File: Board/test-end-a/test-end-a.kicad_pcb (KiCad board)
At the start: 2 copper layers, 150 x 80 mm, 37 parts, among them J10 SW2, J11 TENDA_2, J12 TENDA_1, J2 I2C connector, J5 VAC 230V, J6 VDC 5V, J7 SW1, J8 Anemometer, J9 TX RX - + Serial TTL, K1 FINDER-36.11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

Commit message: [ADD] Add consumption scheme and components on the board
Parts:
- added ACS1: JUMP, Jumper:SolderJumper-2_P1.3mm_Open_RoundedPad1.0x1.5mm, F.Cu at (192.4, 95.0)
- added C3: 1nF, Inductor_SMD:L_1206_3216Metric_Pad1.22x1.90mm_HandSolder, F.Cu at (198.7, 100.6)
- added C4: 56uF, Capacitor_THT:CP_Radial_D10.0mm_P5.00mm, F.Cu at (191.3, 111.8)
- added D4: 1N4148W, Diode_SMD:D_SOD-123, F.Cu at (198.6, 104.0)
- added R13: R100, Resistor_SMD:R_1206_3216Metric, F.Cu at (175.0, 120.1)
- added R14: R10k, Resistor_SMD:R_1206_3216Metric, F.Cu at (178.3, 120.1)
- added R15: R12k, Resistor_SMD:R_1206_3216Metric, F.Cu at (181.6, 120.1)
- added R16: R12k, Resistor_SMD:R_1206_3216Metric, F.Cu at (184.9, 120.1)
- added R17: R10k, Resistor_SMD:R_1206_3216Metric, F.Cu at (188.2, 120.1)
- added R18: R470, Resistor_SMD:R_1206_3216Metric, F.Cu at (191.6, 120.1)
- added R19: R180, Resistor_SMD:R_1206_3216Metric, F.Cu at (194.9, 120.1)
- added U4: ACS712xLCTR-05B, Package_SO:SOIC-8_3.9x4.9mm_P1.27mm, F.Cu at (203.5, 94.0)
- added U5: LM358, Package_SO:SOIC-8-1EP_3.9x4.9mm_P1.27mm_EP2.29x3mm, F.Cu at (211.3, 97.7)
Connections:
- J11 pad 2: /230V_N -> /230V_N_TENDA
- J12 pad 1: /230V_N -> /230V_N_TENDA
- U1 pad 8: unconnected-(U1-IO32-Pad8) -> /ampmeter
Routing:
- net /ampmeter: track 0.00 -> 217.4 mm, vias 0 -> 2
- net /230V_N_TENDA: track 0.00 -> 112.6 mm, vias 0 -> 1
- net GND: track 357.2 -> 467.5 mm, vias 4 -> 5
- net Net-(U4-VIOUT): track 0.00 -> 83.6 mm
- net +5V: track 167.3 -> 238.7 mm, vias 0 -> 5
- net Net-(U5A-+): track 0.00 -> 67.1 mm, vias 0 -> 2
- net Net-(D4-A): track 0.00 -> 62.1 mm
- net Net-(U5A--): track 0.00 -> 58.2 mm, vias 0 -> 2
- net /230V_N: track 115.9 -> 78.9 mm, vias 0 -> 1
- net Net-(D4-K): track 0.00 -> 36.9 mm, vias 0 -> 2
- net Net-(U4-FILTER): track 0.00 -> 11.4 mm
- net Net-(R17-Pad2): track 0.00 -> 7.88 mm, vias 0 -> 2
- net /230V_L: track 100.3 -> 102.9 mm

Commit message: [ENH] Move a wire to avoid interferences with high voltage
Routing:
- net GND: track 467.5 -> 439.1 mm, vias 5 -> 7
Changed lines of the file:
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@@
 			(psa4output no)
 			(plot_black_and_white yes)
+			(plotinvisibletext no)
 			(sketchpadsonfab no)
 			(plotpadnumbers no)
@@
 	)
 	(segment
-		(start 170.615999 133.281)
-		(end 128.281 133.281)
-		(width 0.2)
-		(layer "F.Cu")
-		(net 1)
-	)
-	(segment
 		(start 125.87224 73.46)
 		(end 127.5 73.46)
@@
 	)
 	(segment
-		(start 128.281 133.281)
-		(end 126 131)
-		(width 0.2)
-		(layer "F.Cu")
-		(net 1)
-	)
-	(segment
 		(start 125.6 97.6)
 		(end 122 94)
@@
 	)
 	(segment
-		(start 181.626 121.543)
-		(end 181.626 122.270999)
-		(width 0.2)
-		(layer "F.Cu")
-		(net 1)
-	)
-	(segment
 		(start 205.994 97.748999)
 		(end 206.1415 97.8965)
@@
 	)
 	(segment
+		(start 173.43 121.69066)
+		(end 173.43 111.304)
+		(width 0.2)
+		(layer "F.Cu")
+		(net 1)
+	)
+	(segment
+		(start 180.7625 122.4065)
+		(end 174.14584 122.4065)
+		(width 0.2)
+		(layer "F.Cu")
+		(net 1)
+	)
+	(segment
 		(start 114 131)
 		(end 111.719 133.281)
@@
 	)
 	(segment
+		(start 181.626 121.543)
+		(end 180.7625 122.4065)
+		(width 0.2)
+		(layer "F.Cu")
+		(net 1)
+	)
+	(segment
 		(start 117 86)
 		(end 117 85)
@@
 	)
 	(segment
+		(start 173.43 111.304)
+		(end 175.006 109.728)
+		(width 0.2)
+		(layer "F.Cu")
+		(net 1)
+	)
+	(segment
 		(start 116 117)
 		(end 116.5 117.5)
@@
 	(segment
 		(start 180.605008 99.051)
-		(end 175.848918 99.051)
+		(end 177.546 99.051)
 		(width 0.2)
 		(layer "F.Cu")
@@
 	)
 	(segment
+		(start 177.8 106.934)
+		(end 177.8 99.305)
+		(width 0.2)
+		(layer "F.Cu")
+		(net 1)
+	)
+	(segment
 		(start 106.73 79.660703)
 		(end 106.73 78.205)
@@
 	)
 	(segment
+		(start 177.8 99.305)
+		(end 177.546 99.051)
+		(width 0.2)
+		(layer "F.Cu")
+		(net 1)
+	)
+	(segment
 		(start 97.865 83.2575)
 		(end 103.68 77.4425)
@@
 	)
 	(segment
+		(start 174.14584 122.4065)
+		(end 173.43 121.69066)
+		(width 0.2)
+		(layer "F.Cu")
+		(net 1)
+	)
+	(segment
 		(start 128 97.6)
 		(end 125.6 97.6)
@@
 	)
 	(segment
-		(start 199.136 114.554)
-		(end 200.446 114.554)
+		(start 177.546 99.051)
+		(end 175.848918 99.051)
 		(width 0.2)
 		(layer "F.Cu")
@@
 	)
 	(segment
-		(start 181.626 122.270999)
-		(end 170.615999 133.281)
+		(start 199.136 114.554)
+		(end 200.446 114.554)
 		(width 0.2)
 		(layer "F.Cu")
@@
 	)
 	(via
+		(at 175.006 109.728)
+		(size 0.6)
+		(drill 0.3)
+		(layers "F.Cu" "B.Cu")
+		(net 1)
+	)
+	(via
 		(at 117 86)
 		(size 1)
@@
 	)
 	(via
+		(at 177.8 106.934)
+		(size 0.6)
+		(drill 0.3)
+		(layers "F.Cu" "B.Cu")
+		(net 1)
+	)
+	(via
 		(at 200.66 118.618)
 		(size 0.6)
@@
 	)
 	(segment
+		(start 175.006 109.728)
+		(end 177.8 106.934)
+		(width 0.2)
+		(layer "B.Cu")
+		(net 1)
+	)
+	(segment
 		(start 143.27 93.73)
 		(end 143.27 95)
@@
 	)
 	(segment
-		(start 165.067499 124.000001)
-		(end 169.0675 120)
+		(start 144.999999 131.000001)
+		(end 152 124)
 		(width 2)
 		(layer "F.Cu")
@@
 	)
 	(segment
-		(start 152 124)
-		(end 165.067499 124.000001)
+		(start 145 131)
+		(end 144.999999 131.000001)
+		(width 0.2)
+		(layer "F.Cu")
+		(net 49)
+	)
+	(segment
+		(start 157.625522 124)
+		(end 161.625522 120)
 		(width 2)
 		(layer "F.Cu")
@@
 	)
 	(segment
-		(start 145 131)
-		(end 144.999999 131.000001)
-		(width 0.2)
+		(start 152 124)
+		(end 157.625522 124)
+		(width 2)
 		(layer "F.Cu")
 		(net 49)
 	)
 	(segment
-		(start 144.999999 131.000001)
-		(end 152 124)
+		(start 161.625522 120)
+		(end 169.0675 120)
 		(width 2)
 		(layer "F.Cu")

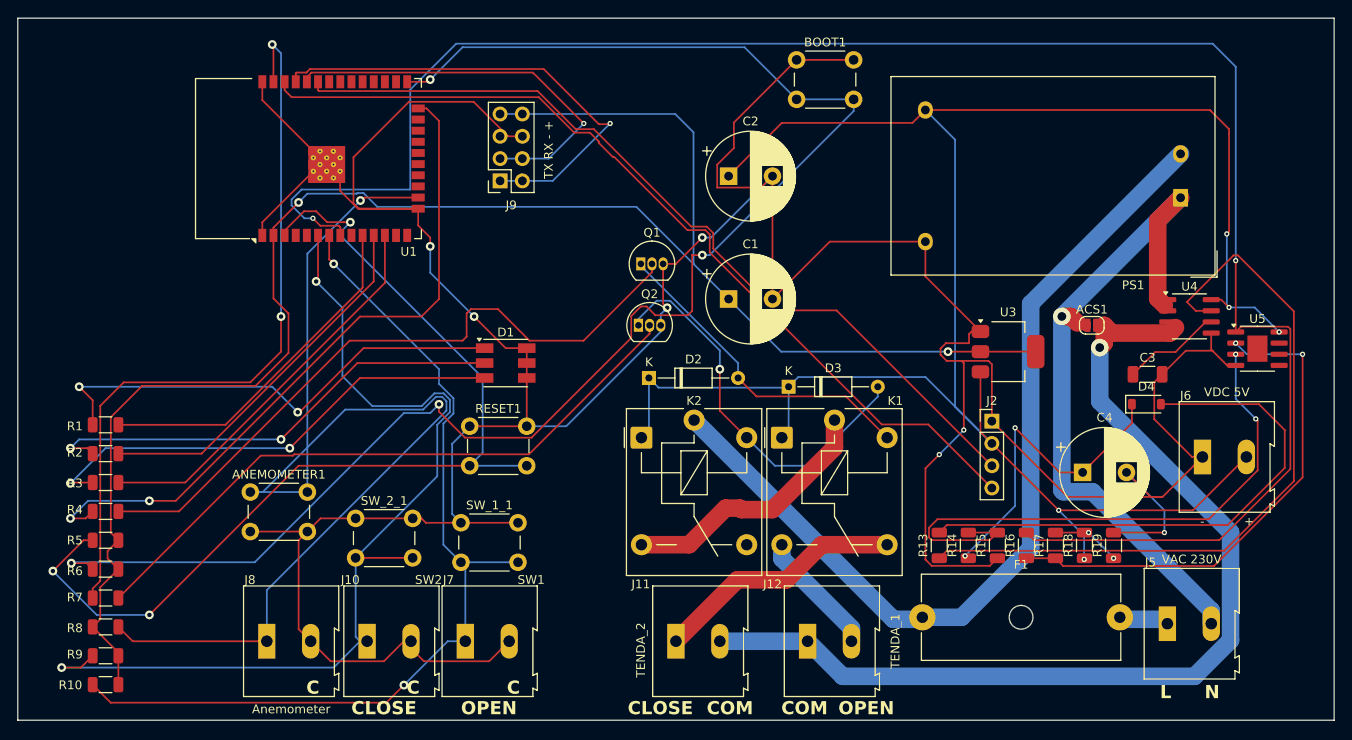
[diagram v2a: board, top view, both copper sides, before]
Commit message: [FIX] Fix board dimensions
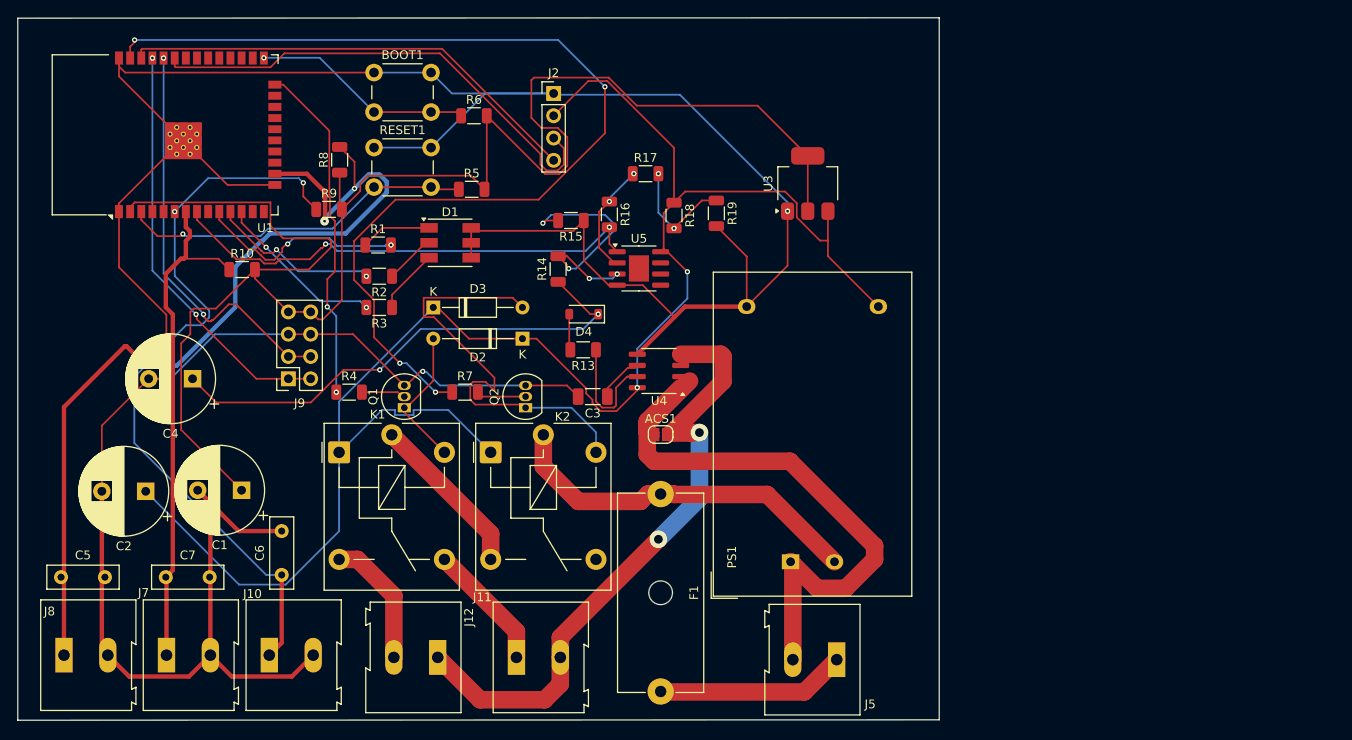
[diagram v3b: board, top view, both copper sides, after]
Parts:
- removed ANEMOMETER1: ANEMOMETER, Button_Switch_THT:SW_PUSH_6mm_H4.3mm
- removed J6: VDC 5V, TerminalBlock:TerminalBlock_Altech_AK300-2_P5.00mm
- removed SW_1_1: SW_1, Button_Switch_THT:SW_PUSH_6mm_H4.3mm
- removed SW_2_1: SW_2, Button_Switch_THT:SW_PUSH_6mm_H4.3mm
- added C5: C, Capacitor_THT:C_Disc_D8.0mm_W2.5mm_P5.00mm, F.Cu at (74.9, 123.7)
- added C6: C, Capacitor_THT:C_Disc_D8.0mm_W2.5mm_P5.00mm, F.Cu at (100.1, 123.4)
- added C7: C, Capacitor_THT:C_Disc_D8.0mm_W2.5mm_P5.00mm, F.Cu at (86.9, 123.7)
- moved C4 102.0 mm to (89.9, 101.1), turned to 180 degrees
- moved C2 75.5 mm to (84.6, 113.9), turned to 180 degrees
- moved U5 71.1 mm to (140.8, 88.5)
- moved R6 66.6 mm to (122.0, 71.1)
- moved D4 64.9 mm to (134.5, 93.7), turned to 180 degrees
- moved C3 63.3 mm to (135.5, 103.1), turned to 180 degrees
- moved R17 63.1 mm to (141.5, 77.7), turned to 0 degrees
- moved J2 62.4 mm to (131.1, 68.6)
- moved R15 61.1 mm to (133.0, 83.1), turned to 180 degrees
- moved PS1 60.8 mm to (158.1, 121.9), turned to 90 degrees
- moved U4 60.8 mm to (143.1, 100.2), turned to 180 degrees
- moved R16 60.7 mm to (137.4, 82.4), turned to -90 degrees
- moved R18 60.0 mm to (144.8, 82.5), turned to -90 degrees
- moved C1 59.6 mm to (95.5, 113.8), turned to 180 degrees
- moved R8 59.5 mm to (106.7, 76.1), turned to 90 degrees
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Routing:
- net /ampmeter: track 217.4 -> 55.6 mm
- net Net-(U1-IO0): track 179.2 -> 25.2 mm, vias 4 -> 1
- net Net-(U1-EN): track 114.0 -> 40.5 mm, vias 3 -> 1
- net Net-(Q1-B): track 77.6 -> 5.04 mm
- net Net-(U4-VIOUT): track 83.6 -> 13.5 mm
- net Net-(Q2-B): track 74.0 -> 5.65 mm
- net /230V_L: track 102.9 -> 42.0 mm
- net Net-(D4-A): track 62.1 -> 4.11 mm
- net GND: track 439.1 -> 384.8 mm, vias 7 -> 2
- net Net-(J2-Pin_4): track 103.2 -> 53.2 mm
- net Net-(D1-RA): track 54.0 -> 5.79 mm, vias 2 -> 0
- net Net-(J7-Pin_1): track 106.3 -> 58.4 mm, vias 2 -> 0
- net Net-(D1-GA): track 54.7 -> 7.41 mm, vias 2 -> 0
- net Net-(D1-BA): track 55.4 -> 8.08 mm, vias 2 -> 0
- net Net-(U5A--): track 58.2 -> 13.0 mm
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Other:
- board size 150 x 80 mm -> 105 x 80 mm
- board text removed: "+"
- board text removed: "-"
- board text removed: "C"
- board text removed: "CLOSE"
- board text removed: "COM"
- board text removed: "L"
- board text removed: "N"
- board text removed: "OPEN"
- board text removed: "TX RX - +"

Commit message: [ADD] Add labels
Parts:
- J9: value TX RX - + Serial TTL -> TX RX - +
- moved C6 2.37 mm to (100.1, 121.1)
- moved C5 2.29 mm to (74.9, 121.4)
- moved C7 1.78 mm to (86.9, 121.9)
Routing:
- net Net-(J10-Pin_1): track 85.8 -> 87.2 mm
- net GND: track 384.8 -> 385.7 mm
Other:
- board text added: "C"
- board text added: "F1"
- board text added: "F2"
- board text added: "L"
- board text added: "N"
